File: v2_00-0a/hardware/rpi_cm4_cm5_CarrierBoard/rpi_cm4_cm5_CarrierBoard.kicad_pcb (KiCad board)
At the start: 2 copper layers, 181.6 x 100.6 mm, 292 parts, among them J1 DM3AT-SF-PEJM5, J19 RPI_CMx_A, J2 0484050003, J3 0484050003, J4 2086581001, J5 0826-1X1T-32-F, Q1 2N7002, Q10 SSM3K56FS,LF, Q11 SSM3K56FS,LF, Q2 2N7002, Q3 2N7002, Q4 2N7002, Q5 2N7002, Q6 2N7002, Q7 2N7002, Q8 2N7002, Q9 DMPH6050SK3-13, U1 STM6710DWB6F, U10 TLV62130ARGTR, U11 TLV62130ARGTR, U12 TPS7A7002DDAR, U13 SE555DR, U14 SN74LVC1G14DBVR, U15 SN65DSI84ZXHR, U16 SN74LVC1G125DBVR, U17 RPI_CMx_B, U18 AP22913W6-7, U2 SN74LVC1G125DBVR, U3 SN74LVC1G125DBVR, U4 AP22913W6-7, U6 SST25VF512A, U7 UPD720202K8-711-BAA-A, U8 AP2192AFGEG-7, U9 TLV62130ARGTR, Y1 24MHz

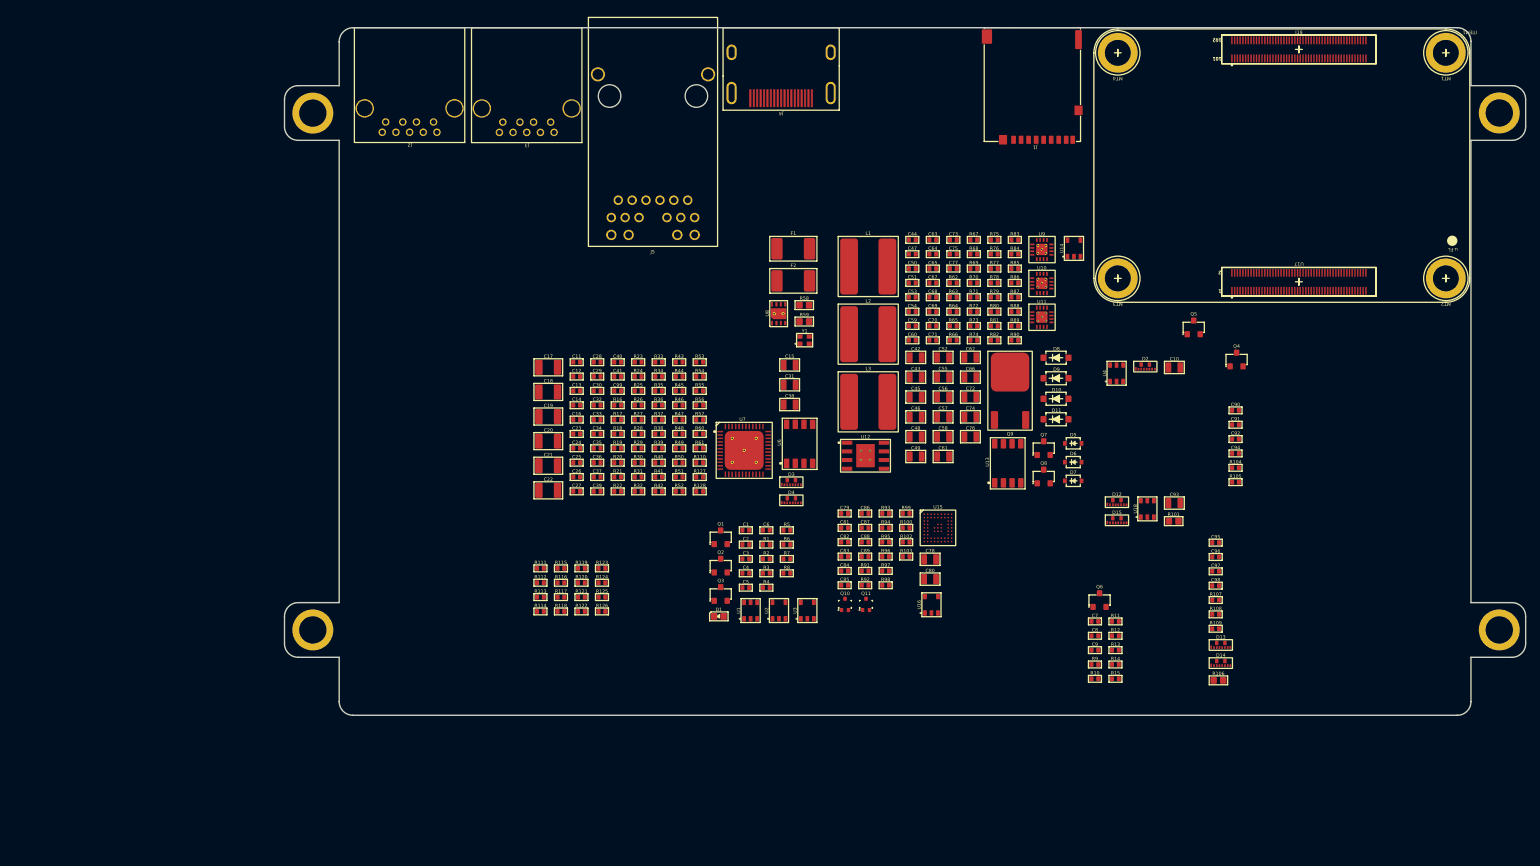
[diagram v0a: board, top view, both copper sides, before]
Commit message: Add new page and update schematics
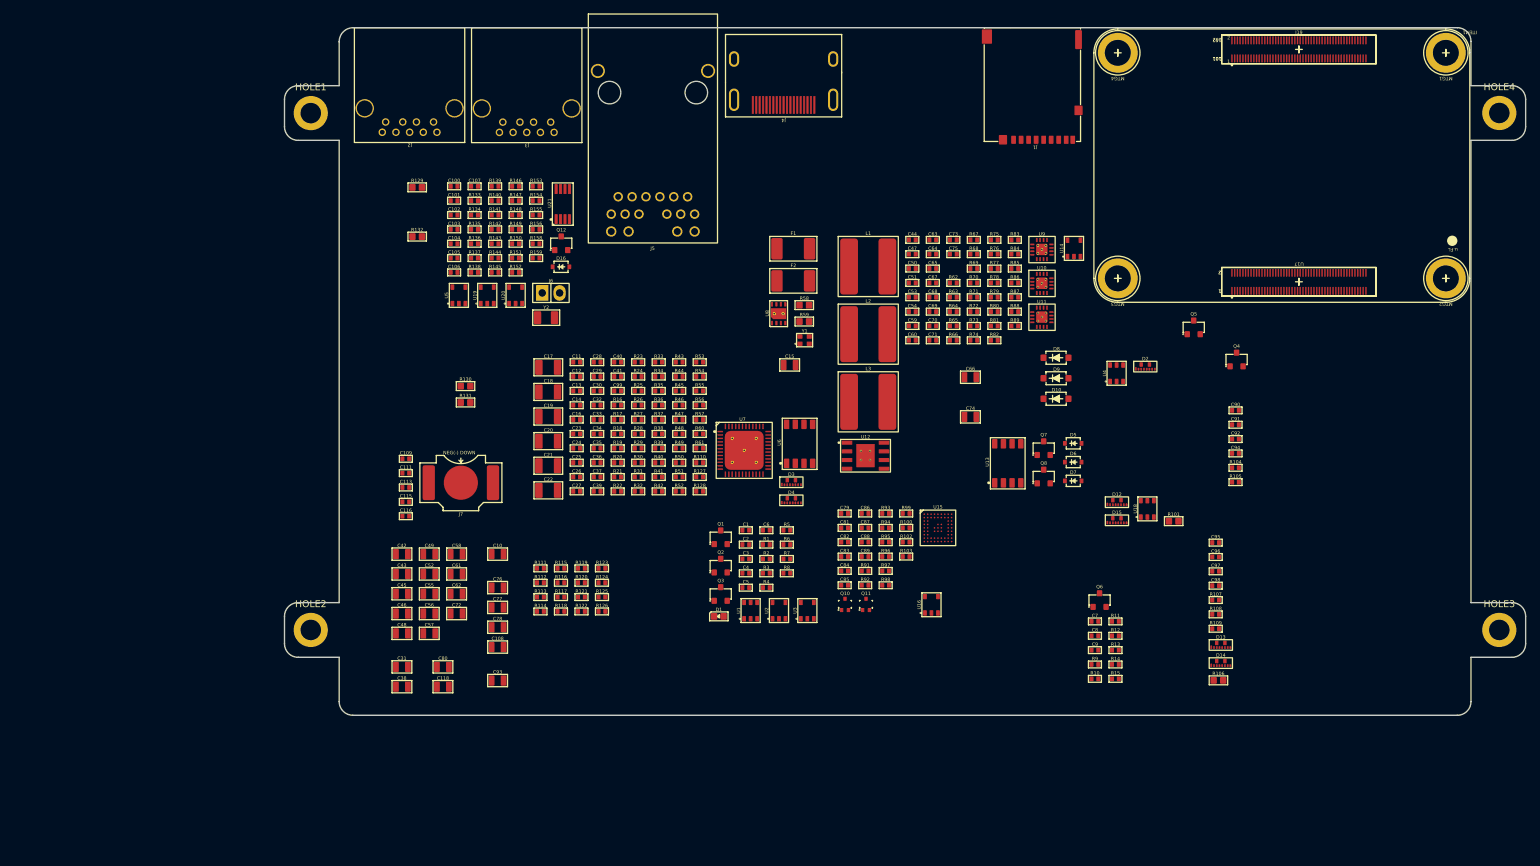
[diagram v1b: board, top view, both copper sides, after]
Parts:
- removed D11: MMSZ5242B, footprint:SOD-123
- removed MT5, MT6, MT7, MT8: M0504-25-AL-7, footprint:M0504-25-AL-7
- removed Q9: DMPH6050SK3-13, footprint:TO-252-3
- removed R90: 12K, footprint:RES_0402
- added C100: 0.1u, footprint:CAP_NONPOL_0402, F.Cu at (84.2, 61.8)
- added C101: 0.1u, footprint:CAP_NONPOL_0402, F.Cu at (84.2, 63.9)
- added C102: 0.1u, footprint:CAP_NONPOL_0402, F.Cu at (84.2, 66.0)
- added C103: 0.1u, footprint:CAP_NONPOL_0402, F.Cu at (84.2, 68.1)
- added C104: 10p, footprint:CAP_NONPOL_0402, F.Cu at (84.2, 70.2)
- added C105: 10p, footprint:CAP_NONPOL_0402, F.Cu at (84.2, 72.3)
- added C106: 0.1u, footprint:CAP_NONPOL_0402, F.Cu at (84.2, 74.4)
- added C107: 0.1u, footprint:CAP_NONPOL_0402, F.Cu at (87.2, 61.8)
- added C108: 22u, footprint:CAP_NONPOL_0805, F.Cu at (90.6, 129.2)
- added C109: 0.1u, footprint:CAP_NONPOL_0402, F.Cu at (77.2, 101.7)
- added C111: 0.1u, footprint:CAP_NONPOL_0402, F.Cu at (77.2, 103.8)
- added C113: 0.1u, footprint:CAP_NONPOL_0402, F.Cu at (77.2, 105.9)
- added C115: 0.1u, footprint:CAP_NONPOL_0402, F.Cu at (77.2, 108.0)
- added C116: 0.1u, footprint:CAP_NONPOL_0402, F.Cu at (77.2, 110.1)
- added C118: 22u, footprint:CAP_NONPOL_0805, F.Cu at (82.6, 135.0)
- added D16: BAT42WS-TP, footprint:SOD-323, F.Cu at (99.9, 73.6)
- added HOLE1: MTG_hole_cir_5mm_pad_3mm_drill, footprint:MTG_hole_cir_5mm_pad_3mm_drill, F.Cu at (63.3, 51.1)
- added HOLE2: MTG_hole_cir_5mm_pad_3mm_drill, footprint:MTG_hole_cir_5mm_pad_3mm_drill, F.Cu at (63.3, 126.7)
- added HOLE3: MTG_hole_cir_5mm_pad_3mm_drill, footprint:MTG_hole_cir_5mm_pad_3mm_drill, F.Cu at (237.2, 126.7)
- added HOLE4: MTG_hole_cir_5mm_pad_3mm_drill, footprint:MTG_hole_cir_5mm_pad_3mm_drill, F.Cu at (237.2, 51.1)
- added J6: M20-9990245, footprint:HEADER_2P_2_54MM, F.Cu at (98.4, 77.4)
- added J7: 2998TR, footprint:2998TR, F.Cu at (85.2, 105.2)
- added MTG5: M0504-25-AL-7, footprint:M0504-25-AL-7, B.Cu at (63.3, 51.1)
- added MTG6: M0504-25-AL-7, footprint:M0504-25-AL-7, B.Cu at (237.2, 51.1)
- added MTG7: M0504-25-AL-7, footprint:M0504-25-AL-7, B.Cu at (63.3, 126.7)
- added MTG8: M0504-25-AL-7, footprint:M0504-25-AL-7, B.Cu at (237.2, 126.7)
- added Q12: 2N7002, footprint:SOT-23-3, F.Cu at (99.9, 70.1)
- added R129: 0R, footprint:RES_0603, F.Cu at (78.8, 62.0)
- added R130: 0R, footprint:RES_0603, F.Cu at (85.9, 91.0)
- added R131: 0R, footprint:RES_0603, F.Cu at (85.9, 93.4)
- added R132: 0R, footprint:RES_0603, F.Cu at (78.8, 69.2)
- added R133: 10K, footprint:RES_0402, F.Cu at (87.2, 63.9)
- added R134: 10K, footprint:RES_0402, F.Cu at (87.2, 66.0)
- added R135: 22R, footprint:RES_0402, F.Cu at (87.2, 68.1)
- added R136: 22R, footprint:RES_0402, F.Cu at (87.2, 70.2)
- added R137: 22R, footprint:RES_0402, F.Cu at (87.2, 72.3)
- added R138: 10K, footprint:RES_0402, F.Cu at (87.2, 74.4)
- added R139: 22R, footprint:RES_0402, F.Cu at (90.2, 61.8)
- added R140: 22R, footprint:RES_0402, F.Cu at (90.2, 63.9)
- added R141: 22R, footprint:RES_0402, F.Cu at (90.2, 66.0)
- added R142: 10K, footprint:RES_0402, F.Cu at (90.2, 68.1)
- added R143: 22R, footprint:RES_0402, F.Cu at (90.2, 70.2)
- added R144: 4K7, footprint:RES_0402, F.Cu at (90.2, 72.3)
- added R145: 4K7, footprint:RES_0402, F.Cu at (90.2, 74.4)
- added R146: 22R, footprint:RES_0402, F.Cu at (93.2, 61.8)
- added R147: 10K, footprint:RES_0402, F.Cu at (93.2, 63.9)
- added R148: 22R, footprint:RES_0402, F.Cu at (93.2, 66.0)
- added R149: 22R, footprint:RES_0402, F.Cu at (93.2, 68.1)
- added R150: 22R, footprint:RES_0402, F.Cu at (93.2, 70.2)
- added R151: 0R, footprint:RES_0402, F.Cu at (93.2, 72.3)
- added R152: 0R, footprint:RES_0402, F.Cu at (93.2, 74.4)
- added R153: 22R, footprint:RES_0402, F.Cu at (96.2, 61.8)
- added R154: 22R, footprint:RES_0402, F.Cu at (96.2, 63.9)
- added R155: 22R, footprint:RES_0402, F.Cu at (96.2, 66.0)
- added R156: 510K, footprint:RES_0402, F.Cu at (96.2, 68.1)
- added R158: 30K1, footprint:RES_0402, F.Cu at (96.2, 70.2)
- added R159: 510K, footprint:RES_0402, F.Cu at (96.2, 72.3)
- added U19: SN74LVC1G125DBVR, footprint:SOT-23-5, F.Cu at (89.1, 77.8)
- added U20: SN74LVC1G07DBVR, footprint:SOT-23-5, F.Cu at (93.2, 77.8)
- added U21: MCP7940NT-I/MS, footprint:MSOP-8, F.Cu at (100.1, 64.4)
- added U5: SN74LVC1G125DBVR, footprint:SOT-23-5, F.Cu at (84.9, 77.8)
- added Y2: 32.768kHz, footprint:2-SMD_3_2mmx1_5mm, F.Cu at (97.7, 81.0)
- C10, C31, C38, C42, C43, C45, C46, C48, C49, C52, C55, C56, C57, C58, C61, C62, C72, C76, C78, C80, C93: value 10u -> 22u
- C77: value 0.1u -> 22u; footprint footprint:CAP_NONPOL_0402 -> footprint:CAP_NONPOL_0805
- moved C10 102.7 mm to (90.6, 115.6)
- moved C93 102.4 mm to (90.6, 134.1)
- moved C77 83.1 mm to (90.6, 123.4)
- moved C62 82.8 mm to (84.6, 121.4)
- moved C52 81.6 mm to (80.6, 118.5)
- moved C55 81.6 mm to (80.6, 121.4)
- moved C56 81.6 mm to (80.6, 124.3)
- moved C57 81.6 mm to (80.6, 127.2)
- moved C72 81.6 mm to (84.6, 124.3)
- moved C42 80.5 mm to (76.6, 115.6)
- moved C43 80.5 mm to (76.6, 118.5)
- moved C45 80.5 mm to (76.6, 121.4)
- moved C46 80.5 mm to (76.6, 124.3)
- moved C48 80.5 mm to (76.6, 127.2)
- moved C58 73.2 mm to (84.6, 115.6)
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- renumbered MT1 to MTG1, MT2 to MTG2, MT3 to MTG3, MT4 to MTG4
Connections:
- net /DSI - LVDS bridge/I2C3.SCL renamed /DSI - LVDS bridge/I2C3.I2C_SCL
- net /DSI - LVDS bridge/I2C3.SDA renamed /DSI - LVDS bridge/I2C3.I2C_SDA
- net /Ethernet/ETH_NLED1 renamed /Ethernet/ETH_~{LED1}
- net /Ethernet/ETH_NLED2 renamed /Ethernet/ETH_~{LED2}
- net /Ethernet/ETH_NLED3 renamed /Ethernet/ETH_~{LED3}
- C76 pad 2: 12V0_CB -> 1V8_CMx
- C77 pad 2: 12V0_CB -> 3V3_CMx
- C78 pad 2: Net-(U15-VCORE) -> 3V3_CB
- J19 pad 10: unconnected-(J19-ETH_P0_N-Pad10) -> /CM4_CM5_CONN_A/ETH_P0_N
- J19 pad 100: unconnected-(J19-~{EXTRST}/GPIO35-Pad100) -> Net-(J19-~{EXTRST}/GPIO35)
- J19 pad 11: unconnected-(J19-ETH_P2_P-Pad11) -> /CM4_CM5_CONN_A/ETH_P2_P
- J19 pad 12: unconnected-(J19-ETH_P0_P-Pad12) -> /CM4_CM5_CONN_A/ETH_P0_P
- J19 pad 15: unconnected-(J19-~{ETH_LED3}-Pad15) -> /CM4_CM5_CONN_A/ETH_~{LED3}
- J19 pad 17: unconnected-(J19-~{ETH_LED2}-Pad17) -> /CM4_CM5_CONN_A/ETH_~{LED2}
- J19 pad 19: unconnected-(J19-~{ETH_LED1}/FAN_PWM-Pad19) -> /CM4_CM5_CONN_A/ETH_~{LED1}
- J19 pad 20: unconnected-(J19-~{EEPROM_WP}-Pad20) -> Net-(J19-~{EEPROM_WP})
- J19 pad 24: unconnected-(J19-GPIO26-Pad24) -> /CM4_CM5_CONN_A/GPIO26
- J19 pad 26: unconnected-(J19-GPIO19-Pad26) -> /CM4_CM5_CONN_A/GPIO19
- J19 pad 28: unconnected-(J19-GPIO13-Pad28) -> /CM4_CM5_CONN_A/WDOG_IN
- J19 pad 3: unconnected-(J19-ETH_P3_P-Pad3) -> /CM4_CM5_CONN_A/ETH_P3_P
- J19 pad 30: unconnected-(J19-GPIO6-Pad30) -> /CM4_CM5_CONN_A/GPIO6
- J19 pad 34: unconnected-(J19-GPIO5-Pad34) -> /CM4_CM5_CONN_A/I2C3.I2C_SCL
- J19 pad 38: unconnected-(J19-GPIO11-Pad38) -> /CM4_CM5_CONN_A/GPIO11
- J19 pad 4: unconnected-(J19-ETH_P1_P-Pad4) -> /CM4_CM5_CONN_A/ETH_P1_P
- J19 pad 40: unconnected-(J19-GPIO9-Pad40) -> /CM4_CM5_CONN_A/SPI2.SPI_MISO
- J19 pad 44: unconnected-(J19-GPIO10-Pad44) -> /CM4_CM5_CONN_A/GPIO10
- J19 pad 48: unconnected-(J19-GPIO27-Pad48) -> /CM4_CM5_CONN_A/GPIO27
- J19 pad 5: unconnected-(J19-ETH_P3_N-Pad5) -> /CM4_CM5_CONN_A/ETH_P3_N
- J19 pad 50: unconnected-(J19-GPIO17-Pad50) -> /CM4_CM5_CONN_A/GPIO17
- J19 pad 54: unconnected-(J19-GPIO4-Pad54) -> /CM4_CM5_CONN_A/I2C3.I2C_SDA
- J19 pad 57: unconnected-(J19-SD_CLK-Pad57) -> /CM4_CM5_CONN_A/SDIO_CLK
- J19 pad 6: unconnected-(J19-ETH_P1_N-Pad6) -> /CM4_CM5_CONN_A/ETH_P3_N
- J19 pad 61: unconnected-(J19-SD_DAT3-Pad61) -> /CM4_CM5_CONN_A/SDIO_D3
- J19 pad 62: unconnected-(J19-SD_CMD-Pad62) -> /CM4_CM5_CONN_A/SDIO_CMD
- J19 pad 63: unconnected-(J19-SD_DAT0-Pad63) -> /CM4_CM5_CONN_A/SDIO_D0
- J19 pad 67: unconnected-(J19-SD_DAT1-Pad67) -> /CM4_CM5_CONN_A/SDIO_D1
- J19 pad 69: unconnected-(J19-SD_DAT2-Pad69) -> /CM4_CM5_CONN_A/SDIO_D2
- J19 pad 75: unconnected-(J19-SD_PWR_ON-Pad75) -> Net-(J19-SD_PWR_ON)
- J19 pad 77: unconnected-(J19-+5V-Pad77) -> 3V3_CB
- J19 pad 78: unconnected-(J19-GPIO_VREF-Pad78) -> /CM4_CM5_CONN_A/GPIO_VREF
- J19 pad 79: unconnected-(J19-+5V-Pad79) -> 3V3_CB
- J19 pad 80: unconnected-(J19-SCL0-Pad80) -> /CM4_CM5_CONN_A/I2C0.I2C_SCL
- J19 pad 81: unconnected-(J19-+5V-Pad81) -> 3V3_CB
- J19 pad 82: unconnected-(J19-SDA0-Pad82) -> /CM4_CM5_CONN_A/I2C0.I2C_SDA
- J19 pad 83: unconnected-(J19-+5V-Pad83) -> 3V3_CB
- J19 pad 84: unconnected-(J19-CM4_3V3_OUT-Pad84) -> 3V3_CMx
- J19 pad 85: unconnected-(J19-+5V-Pad85) -> 3V3_CB
- J19 pad 86: unconnected-(J19-CM4_3V3_OUT-Pad86) -> 3V3_CMx
- J19 pad 87: unconnected-(J19-+5V-Pad87) -> 3V3_CB
- J19 pad 88: unconnected-(J19-CM4_1V8_OUT-Pad88) -> 1V8_CMx
- J19 pad 9: unconnected-(J19-ETH_P2_N-Pad9) -> /CM4_CM5_CONN_A/ETH_P2_N
- J19 pad 90: unconnected-(J19-CM4_1V8_OUT-Pad90) -> 1V8_CMx
- J19 pad 92: unconnected-(J19-RUN_PG/PWR_BTN-Pad92) -> Net-(J19-RUN_PG/PWR_BTN)
- J19 pad 93: unconnected-(J19-~{RPIBOOT}-Pad93) -> Net-(J19-~{RPIBOOT})
- J19 pad 95: unconnected-(J19-~{PI_LED_PWR}-Pad95) -> Net-(J19-~{PI_LED_PWR})
- J19 pad 97: unconnected-(J19-CAM_GPIO/GPIO34-Pad97) -> Net-(J19-CAM_GPIO/GPIO34)
- J19 pad 99: unconnected-(J19-GLOBAL_EN/PMIC_EN-Pad99) -> Net-(J19-GLOBAL_EN/PMIC_EN)
- R62 pad 1: 3V3_CM4 -> 3V3_CMx
- U14 pad 2: 3V3_CM4 -> 3V3_CMx

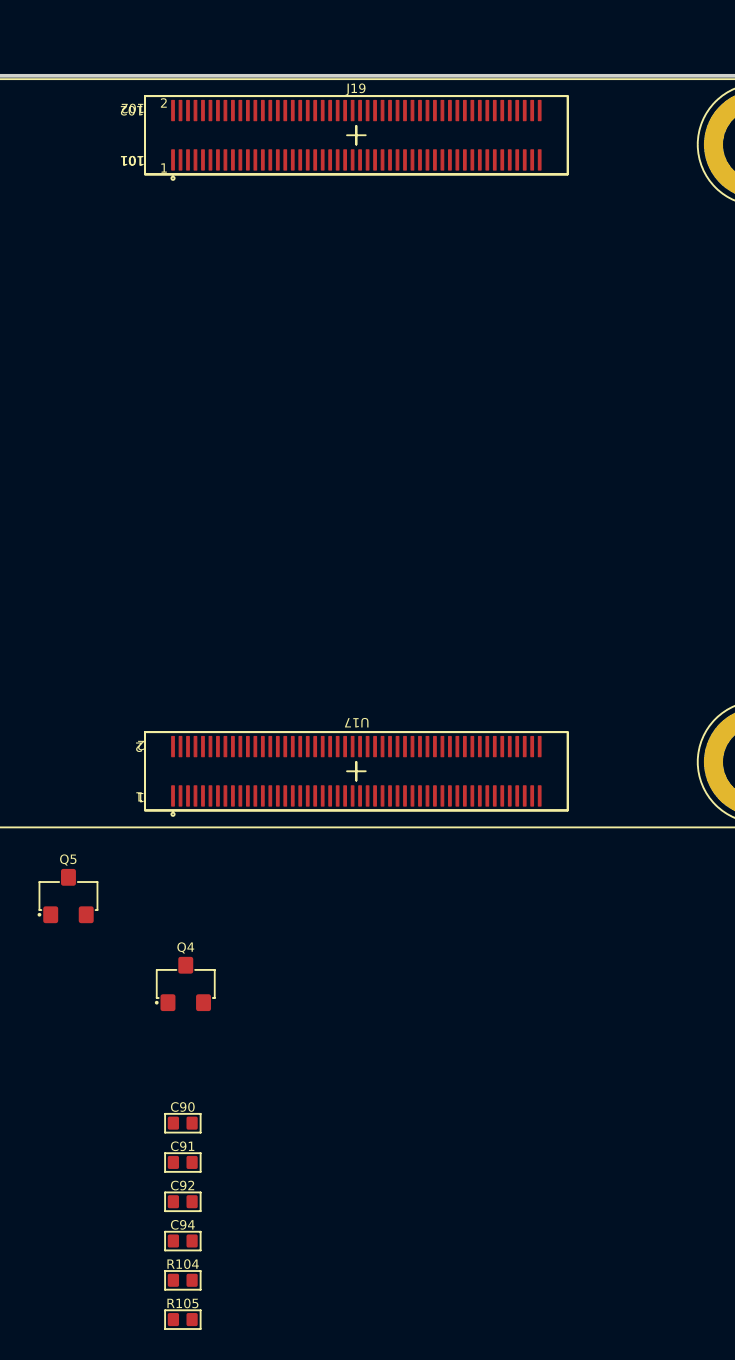
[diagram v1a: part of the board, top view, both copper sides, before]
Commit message: Add design notes (power table) and latest changes to power supply and power input
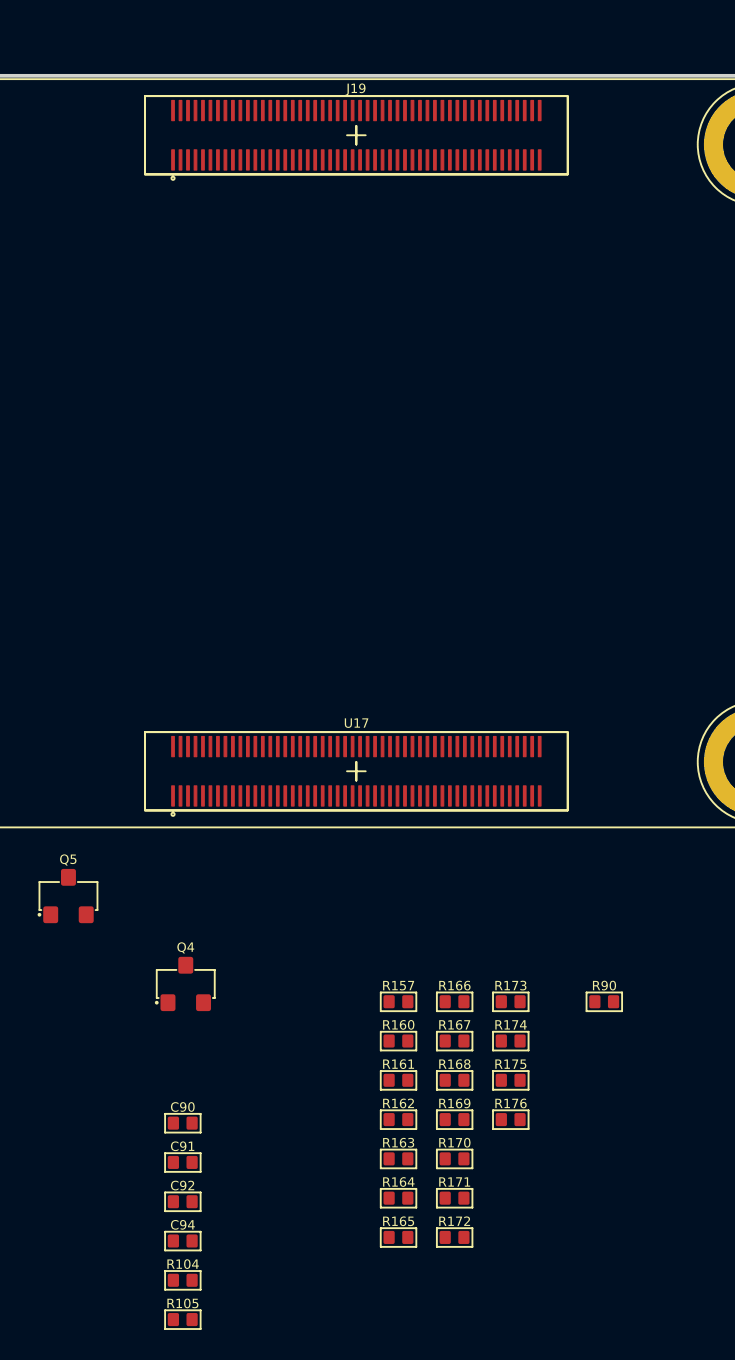
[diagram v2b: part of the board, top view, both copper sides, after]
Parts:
- added R157: 0R, footprint:RES_0402, F.Cu at (210.1, 88.1)
- added R160: 0R, footprint:RES_0402, F.Cu at (210.1, 90.2)
- added R161: 0R, footprint:RES_0402, F.Cu at (210.1, 92.3)
- added R162: 0R, footprint:RES_0402, F.Cu at (210.1, 94.4)
- added R163: 0R, footprint:RES_0402, F.Cu at (210.1, 96.5)
- added R164: 0R, footprint:RES_0402, F.Cu at (210.1, 98.6)
- added R165: 0R, footprint:RES_0402, F.Cu at (210.1, 100.7)
- added R166: 0R, footprint:RES_0402, F.Cu at (213.1, 88.1)
- added R167: 0R, footprint:RES_0402, F.Cu at (213.1, 90.2)
- added R168: 0R, footprint:RES_0402, F.Cu at (213.1, 92.3)
- added R169: 0R, footprint:RES_0402, F.Cu at (213.1, 94.4)
- added R170: 0R, footprint:RES_0402, F.Cu at (213.1, 96.5)
- added R171: 0R, footprint:RES_0402, F.Cu at (213.1, 98.6)
- added R172: 0R, footprint:RES_0402, F.Cu at (213.1, 100.7)
- added R173: 0R, footprint:RES_0402, F.Cu at (216.1, 88.1)
- added R174: 0R, footprint:RES_0402, F.Cu at (216.1, 90.2)
- added R175: 0R, footprint:RES_0402, F.Cu at (216.1, 92.3)
- added R176: 0R, footprint:RES_0402, F.Cu at (216.1, 94.4)
- added R90: 10K, footprint:RES_0402, F.Cu at (221.1, 88.1)
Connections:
- net /HDMI/HDMI_CEC renamed /HDMI/HDMI0.CEC
- net /HDMI/HDMI_CLK_N renamed /HDMI/HDMI0.CLK_N
- net /HDMI/HDMI_CLK_P renamed /HDMI/HDMI0.CLK_P
- net /HDMI/HDMI_D0_N renamed /HDMI/HDMI0.D0_N
- net /HDMI/HDMI_D0_P renamed /HDMI/HDMI0.D0_P
- net /HDMI/HDMI_D1_N renamed /HDMI/HDMI0.D1_N
- net /HDMI/HDMI_D1_P renamed /HDMI/HDMI0.D1_P
- net /HDMI/HDMI_D2_N renamed /HDMI/HDMI0.D2_N
- net /HDMI/HDMI_D2_P renamed /HDMI/HDMI0.D2_P
- net /HDMI/HDMI_HPD renamed /HDMI/HDMI0.HPD
- net /HDMI/HDMI_SCL renamed /HDMI/HDMI0.SCL
- net /HDMI/HDMI_SDA renamed /HDMI/HDMI0.SDA
- net /USB_3/PCIE_CLK_N renamed /USB_3/USB_HUB.CLK_N
- net /USB_3/PCIE_CLK_P renamed /USB_3/USB_HUB.CLK_P
- net /USB_3/PCIE_CLK_~{REQ} renamed /USB_3/USB_HUB.~{REQ}
- net /USB_3/PCIE_RX_N renamed /USB_3/USB_HUB.RX_N
- net /USB_3/PCIE_RX_P renamed /USB_3/USB_HUB.RX_P
- net /USB_3/PCIE_TX_N renamed /USB_3/USB_HUB.TX_N
- net /USB_3/PCIE_TX_P renamed /USB_3/USB_HUB.TX_P
- net /USB_3/PCIE_~{RST} renamed /USB_3/USB_HUB.~{RST}
- net /USB_3/PCIE_~{WAKE} renamed /USB_3/USB_HUB.~{WAKE}
- U15 pad A3: unconnected-(U15-B_Y0N-PadA3) -> /DSI - LVDS bridge/LVDS_B.D0_N
- U15 pad A4: unconnected-(U15-B_Y1N-PadA4) -> /DSI - LVDS bridge/LVDS_B.D1_N
- U15 pad A5: unconnected-(U15-B_Y2N-PadA5) -> /DSI - LVDS bridge/LVDS_B.D2_N
- U15 pad A6: unconnected-(U15-B_CLKN-PadA6) -> /DSI - LVDS bridge/LVDS_B.CLK_N
- U15 pad A7: unconnected-(U15-B_Y3N-PadA7) -> /DSI - LVDS bridge/LVDS_B.D3_N
- U15 pad B3: unconnected-(U15-B_Y0P-PadB3) -> /DSI - LVDS bridge/LVDS_B.D0_P
- U15 pad B4: unconnected-(U15-B_Y1P-PadB4) -> /DSI - LVDS bridge/LVDS_B.D1_P
- U15 pad B5: unconnected-(U15-B_Y2P-PadB5) -> /DSI - LVDS bridge/LVDS_B.D2_P
- U15 pad B6: unconnected-(U15-B_CLKP-PadB6) -> /DSI - LVDS bridge/LVDS_B.CLK_P
- U15 pad B7: unconnected-(U15-B_Y3P-PadB7) -> /DSI - LVDS bridge/LVDS_B.D3_P
- U15 pad C8: unconnected-(U15-A_Y0P-PadC8) -> /DSI - LVDS bridge/LVDS_A.D0_P
- U15 pad C9: unconnected-(U15-A_Y0N-PadC9) -> /DSI - LVDS bridge/LVDS_A.D0_N
- U15 pad D8: unconnected-(U15-A_Y1P-PadD8) -> /DSI - LVDS bridge/LVDS_A.D1_P
- U15 pad D9: unconnected-(U15-A_Y1N-PadD9) -> /DSI - LVDS bridge/LVDS_A.D1_N
- U15 pad E8: unconnected-(U15-A_Y2P-PadE8) -> /DSI - LVDS bridge/LVDS_A.D2_P
- U15 pad E9: unconnected-(U15-A_Y2N-PadE9) -> /DSI - LVDS bridge/LVDS_A.D2_N
- U15 pad F8: unconnected-(U15-A_CLKP-PadF8) -> /DSI - LVDS bridge/LVDS_A.CLK_P
- U15 pad F9: unconnected-(U15-A_CLKN-PadF9) -> /DSI - LVDS bridge/LVDS_A.CLK_N
- U15 pad G8: unconnected-(U15-A_Y3P-PadG8) -> /DSI - LVDS bridge/LVDS_A.D3_P
- U15 pad G9: unconnected-(U15-A_Y3N-PadG9) -> /DSI - LVDS bridge/LVDS_A.D3_N
- U15 pad H3: unconnected-(U15-DA0P-PadH3) -> /DSI - LVDS bridge/DSI1.D0_P
- U15 pad H4: unconnected-(U15-DA1P-PadH4) -> /DSI - LVDS bridge/DSI1.D1_P
- U15 pad H5: unconnected-(U15-DACP-PadH5) -> /DSI - LVDS bridge/DSI1.CLK_P
- U15 pad H6: unconnected-(U15-DA2P-PadH6) -> /DSI - LVDS bridge/DSI1.D2_P
- U15 pad H7: unconnected-(U15-DA3P-PadH7) -> /DSI - LVDS bridge/DSI1.D3_P
- U15 pad J3: unconnected-(U15-DA0N-PadJ3) -> /DSI - LVDS bridge/DSI1.D0_N
- U15 pad J4: unconnected-(U15-DA1N-PadJ4) -> /DSI - LVDS bridge/DSI1.D1_N
- U15 pad J5: unconnected-(U15-DACN-PadJ5) -> /DSI - LVDS bridge/DSI1.CLK_N
- U15 pad J6: unconnected-(U15-DA2N-PadJ6) -> /DSI - LVDS bridge/DSI1.D2_N
- U15 pad J7: unconnected-(U15-DA3N-PadJ7) -> /DSI - LVDS bridge/DSI1.D3_N
- U17 pad 1: unconnected-(U17-USB_OTG_ID-Pad1) -> /CM4_CM5_CONN_B/USB.OTG_ID
- U17 pad 10: unconnected-(U17-PCIe_CLK_P-Pad10) -> /CM4_CM5_CONN_B/PCIe_CLK_P
- U17 pad 100: unconnected-(U17-HDMI0_SCL-Pad100) -> /CM4_CM5_CONN_B/HDMI0.SCL
- U17 pad 11: unconnected-(U17-VDAC_COMP/VBUS_EN-Pad11) -> /CM4_CM5_CONN_B/CM5_USB3_VBUS_EN
- U17 pad 12: unconnected-(U17-PCIe_CLK_N-Pad12) -> /CM4_CM5_CONN_B/PCIe_CLK_N
- U17 pad 13: unconnected-(U17-GND-Pad13) -> GND
- U17 pad 14: unconnected-(U17-GND-Pad14) -> GND
- U17 pad 15: unconnected-(U17-CAM1_D0_N-Pad15) -> /CM4_CM5_CONN_B/CSI1.D0_N
- U17 pad 16: unconnected-(U17-PCIe_RX_P-Pad16) -> /CM4_CM5_CONN_B/PCIe_RX_P
- U17 pad 17: unconnected-(U17-CAM1_D0_P-Pad17) -> /CM4_CM5_CONN_B/CSI1.D0_P
- U17 pad 18: unconnected-(U17-PCIe_RX_N-Pad18) -> /CM4_CM5_CONN_B/PCIe_RX_N
- U17 pad 19: unconnected-(U17-GND-Pad19) -> GND
- U17 pad 2: unconnected-(U17-~{PCIe_CLK_REQ}-Pad2) -> /CM4_CM5_CONN_B/PCIe_CLK_~{REQ}
- U17 pad 20: unconnected-(U17-GND-Pad20) -> GND
- U17 pad 21: unconnected-(U17-CAM1_D1_N-Pad21) -> /CM4_CM5_CONN_B/CSI1.D1_N
- U17 pad 22: unconnected-(U17-PCIe_TX_P-Pad22) -> /CM4_CM5_CONN_B/PCIe_TX_P
- U17 pad 23: unconnected-(U17-CAM1_D1_P-Pad23) -> /CM4_CM5_CONN_B/CSI1.D1_P
- U17 pad 24: unconnected-(U17-PCIe_TX_N-Pad24) -> /CM4_CM5_CONN_B/PCIe_TX_N
- U17 pad 25: unconnected-(U17-GND-Pad25) -> GND
- U17 pad 26: unconnected-(U17-GND-Pad26) -> GND
- U17 pad 27: unconnected-(U17-CAM1_CLK_N-Pad27) -> /CM4_CM5_CONN_B/CSI1.CLK_N
- U17 pad 28: unconnected-(U17-CAM0_D0_N/USB3_0_RX_N-Pad28) -> /CM4_CM5_CONN_B/CM5_USB3_0.U3RXD_N
- U17 pad 29: unconnected-(U17-CAM1_CLK_P-Pad29) -> /CM4_CM5_CONN_B/CSI1.CLK_P
- U17 pad 3: unconnected-(U17-USB_N-Pad3) -> /CM4_CM5_CONN_B/USB.USB_N
- U17 pad 30: unconnected-(U17-CAM0_D0_P/USB3_0_RX_P-Pad30) -> /CM4_CM5_CONN_B/CM5_USB3_0.U3RXD_P
- U17 pad 31: unconnected-(U17-GND-Pad31) -> GND
- U17 pad 32: unconnected-(U17-GND-Pad32) -> GND
- U17 pad 33: unconnected-(U17-CAM1_D2_N-Pad33) -> /CM4_CM5_CONN_B/CSI1.D2_N
- U17 pad 34: unconnected-(U17-CAM0_D1_N/USB3_0_P-Pad34) -> /CM4_CM5_CONN_B/CM5_USB3_0.USB_P
- U17 pad 35: unconnected-(U17-CAM1_D2_P-Pad35) -> /CM4_CM5_CONN_B/CSI1.D2_P
- U17 pad 36: unconnected-(U17-CAM0_D1_P/USB3_0_N-Pad36) -> /CM4_CM5_CONN_B/CM5_USB3_0.USB_N
- U17 pad 37: unconnected-(U17-GND-Pad37) -> GND
- U17 pad 38: unconnected-(U17-GND-Pad38) -> GND
- U17 pad 39: unconnected-(U17-CAM1_D3_N-Pad39) -> /CM4_CM5_CONN_B/CSI1.D3_N
- U17 pad 4: unconnected-(U17-RSVD/~{PCIe_DET_WAKE}-Pad4) -> /CM4_CM5_CONN_B/PCIe_~{WAKE}
- U17 pad 40: unconnected-(U17-CAM0_CLK_N/USB3_0_TX_N-Pad40) -> /CM4_CM5_CONN_B/CM5_USB3_0.U3TXD_N
- U17 pad 41: unconnected-(U17-CAM1_D3_P-Pad41) -> /CM4_CM5_CONN_B/CSI1.D3_P
- U17 pad 42: unconnected-(U17-CAM0_CLK_P/USB3_0_TX_P-Pad42) -> /CM4_CM5_CONN_B/CM5_USB3_0.U3TXD_P
- U17 pad 44: unconnected-(U17-GND-Pad44) -> GND
- U17 pad 5: unconnected-(U17-USB_P-Pad5) -> /CM4_CM5_CONN_B/USB.USB_P
- U17 pad 50: unconnected-(U17-GND-Pad50) -> GND
- U17 pad 51: unconnected-(U17-HDMI0_CEC-Pad51) -> /CM4_CM5_CONN_B/HDMI0.CEC
- U17 pad 53: unconnected-(U17-HDMI0_HPD-Pad53) -> /CM4_CM5_CONN_B/HDMI0.HPD
- U17 pad 55: unconnected-(U17-GND-Pad55) -> GND
- U17 pad 56: unconnected-(U17-GND-Pad56) -> GND
- U17 pad 57: unconnected-(U17-DSI0_D0_N/USB3_1_RX_N-Pad57) -> /CM4_CM5_CONN_B/CM5_USB3_1.U3RXD_N
- U17 pad 59: unconnected-(U17-DSI0_D0_P/USB3_1_RX_P-Pad59) -> /CM4_CM5_CONN_B/CM5_USB3_1.U3RXD_P
- U17 pad 61: unconnected-(U17-GND-Pad61) -> GND
- U17 pad 62: unconnected-(U17-GND-Pad62) -> GND
- U17 pad 63: unconnected-(U17-DSI0_D1_N/USB3_1_P-Pad63) -> /CM4_CM5_CONN_B/CM5_USB3_1.USB_P
- U17 pad 65: unconnected-(U17-DSI0_D1_P/USB3_1_N-Pad65) -> /CM4_CM5_CONN_B/CM5_USB3_1.USB_N
- U17 pad 67: unconnected-(U17-GND-Pad67) -> GND
- U17 pad 68: unconnected-(U17-GND-Pad68) -> GND
- U17 pad 69: unconnected-(U17-DSI0_CLK_N//USB3_1_TX_N-Pad69) -> /CM4_CM5_CONN_B/CM5_USB3_1.U3TXD_N
- U17 pad 7: unconnected-(U17-GND-Pad7) -> GND
- U17 pad 70: unconnected-(U17-HDMI0_TX2_P-Pad70) -> /CM4_CM5_CONN_B/HDMI0.D2_P
- U17 pad 71: unconnected-(U17-DSI0_CLK_P/USB3_1_TX_P-Pad71) -> /CM4_CM5_CONN_B/CM5_USB3_1.U3TXD_P
- U17 pad 72: unconnected-(U17-HDMI0_TX2_N-Pad72) -> /CM4_CM5_CONN_B/HDMI0.D2_N
- U17 pad 73: unconnected-(U17-GND-Pad73) -> GND
- U17 pad 74: unconnected-(U17-GND-Pad74) -> GND
- U17 pad 75: unconnected-(U17-DSI1_D0_N-Pad75) -> /CM4_CM5_CONN_B/DSI1.D0_N
- U17 pad 76: unconnected-(U17-HDMI0_TX1_P-Pad76) -> /CM4_CM5_CONN_B/HDMI0.D1_P
- U17 pad 77: unconnected-(U17-DSI1_D0_P-Pad77) -> /CM4_CM5_CONN_B/DSI1.D0_P
- U17 pad 78: unconnected-(U17-HDMI0_TX1_N-Pad78) -> /CM4_CM5_CONN_B/HDMI0.D1_N
- U17 pad 79: unconnected-(U17-GND-Pad79) -> GND
- U17 pad 8: unconnected-(U17-GND-Pad8) -> GND
- U17 pad 80: unconnected-(U17-GND-Pad80) -> GND
- U17 pad 81: unconnected-(U17-DSI1_D1_N-Pad81) -> /CM4_CM5_CONN_B/DSI1.D1_N
- U17 pad 82: unconnected-(U17-HDMI0_TX0_P-Pad82) -> /CM4_CM5_CONN_B/HDMI0.D0_P
- U17 pad 83: unconnected-(U17-DSI1_D1_P-Pad83) -> /CM4_CM5_CONN_B/DSI1.D1_P
- U17 pad 84: unconnected-(U17-HDMI0_TX0_N-Pad84) -> /CM4_CM5_CONN_B/HDMI0.D0_N
- U17 pad 85: unconnected-(U17-GND-Pad85) -> GND
- U17 pad 86: unconnected-(U17-GND-Pad86) -> GND
- U17 pad 87: unconnected-(U17-DSI1_CLK_N-Pad87) -> /CM4_CM5_CONN_B/DSI1.CLK_N
- U17 pad 88: unconnected-(U17-HDMI0_CLK_P-Pad88) -> /CM4_CM5_CONN_B/HDMI0.CLK_P
- U17 pad 89: unconnected-(U17-DSI1_CLK_P-Pad89) -> /CM4_CM5_CONN_B/DSI1.CLK_P
- U17 pad 9: unconnected-(U17-~{PCIe_RST}-Pad9) -> /CM4_CM5_CONN_B/PCIe_~{RST}
- U17 pad 90: unconnected-(U17-HDMI0_CLK_N-Pad90) -> /CM4_CM5_CONN_B/HDMI0.CLK_N
- U17 pad 91: unconnected-(U17-GND-Pad91) -> GND
- U17 pad 92: unconnected-(U17-GND-Pad92) -> GND
- U17 pad 93: unconnected-(U17-DSI1_D2_N-Pad93) -> /CM4_CM5_CONN_B/DSI1.D2_N
- U17 pad 94: unconnected-(U17-DSI1_D3_N-Pad94) -> /CM4_CM5_CONN_B/DSI1.D3_N
- U17 pad 95: unconnected-(U17-DSI1_D2_P-Pad95) -> /CM4_CM5_CONN_B/DSI1.D2_P
- U17 pad 96: unconnected-(U17-DSI1_D3_P-Pad96) -> /CM4_CM5_CONN_B/DSI1.D3_P
- U17 pad 97: unconnected-(U17-GND-Pad97) -> GND
- U17 pad 98: unconnected-(U17-GND-Pad98) -> GND
- U17 pad 99: unconnected-(U17-HDMI0_SDA-Pad99) -> /CM4_CM5_CONN_B/HDMI0.SDA
